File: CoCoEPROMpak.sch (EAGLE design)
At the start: 5 parts, among them P1 COCO-CART, U1 2732, U2 27128

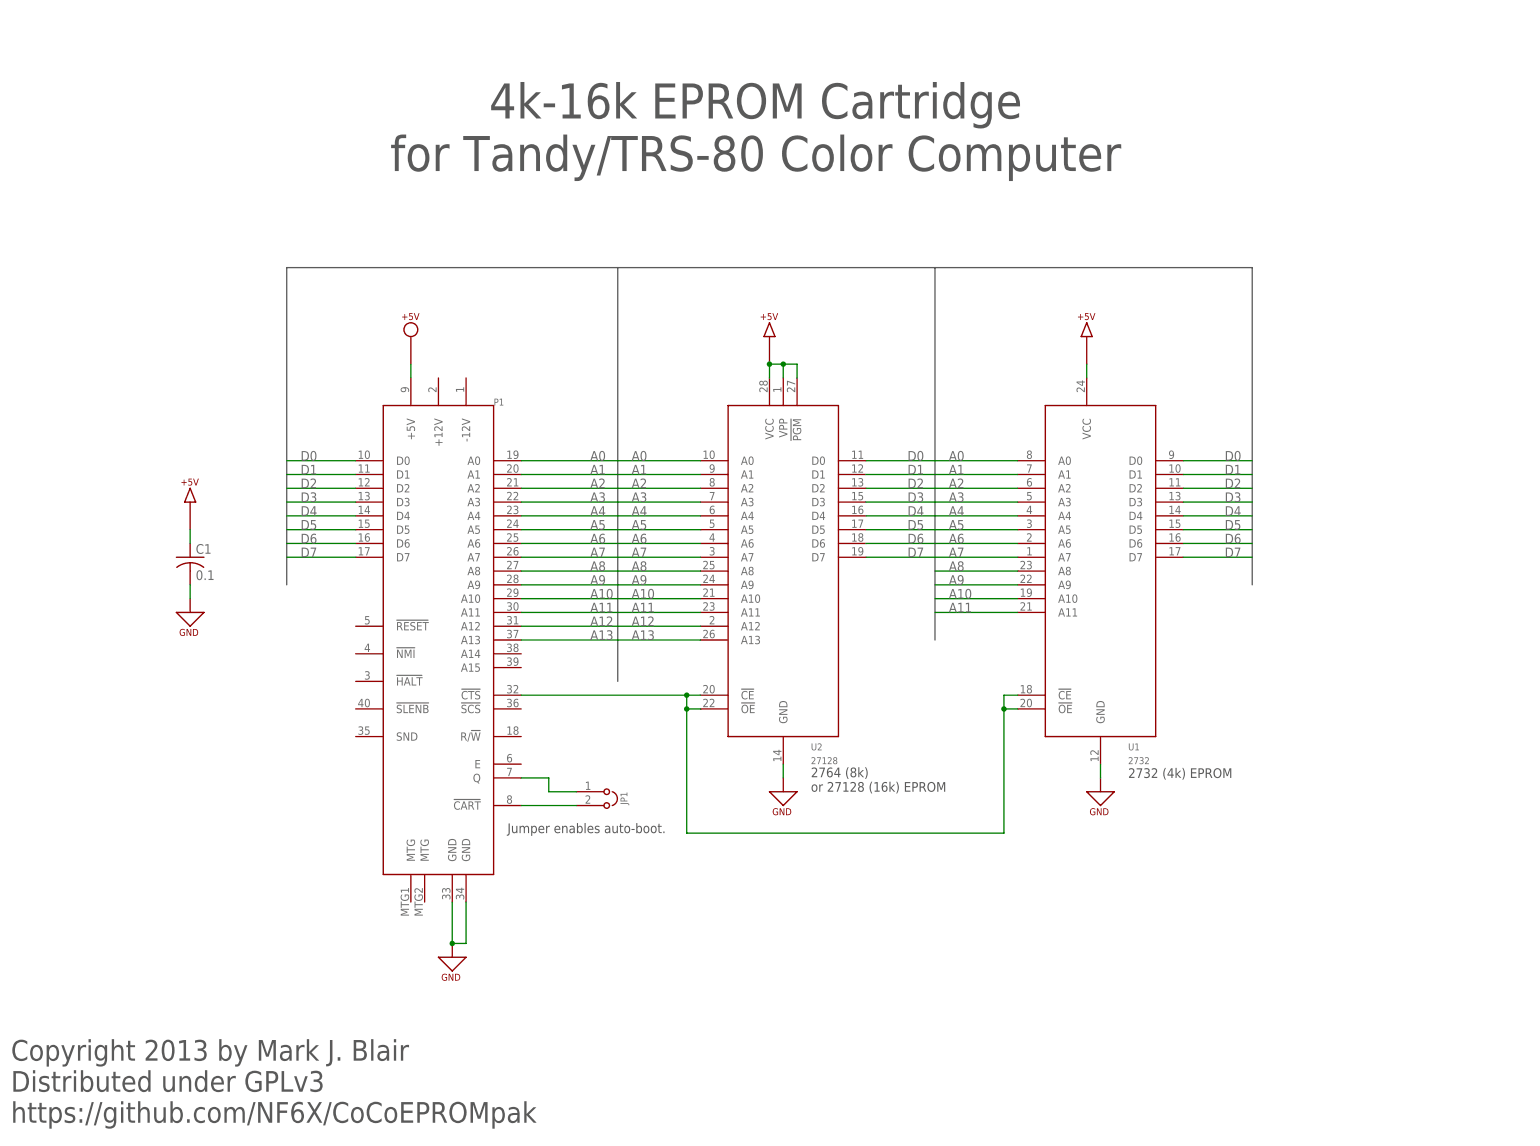
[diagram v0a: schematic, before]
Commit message: Added support for 27256 and 27512 EPROMs with bank-switching by jumper settings.
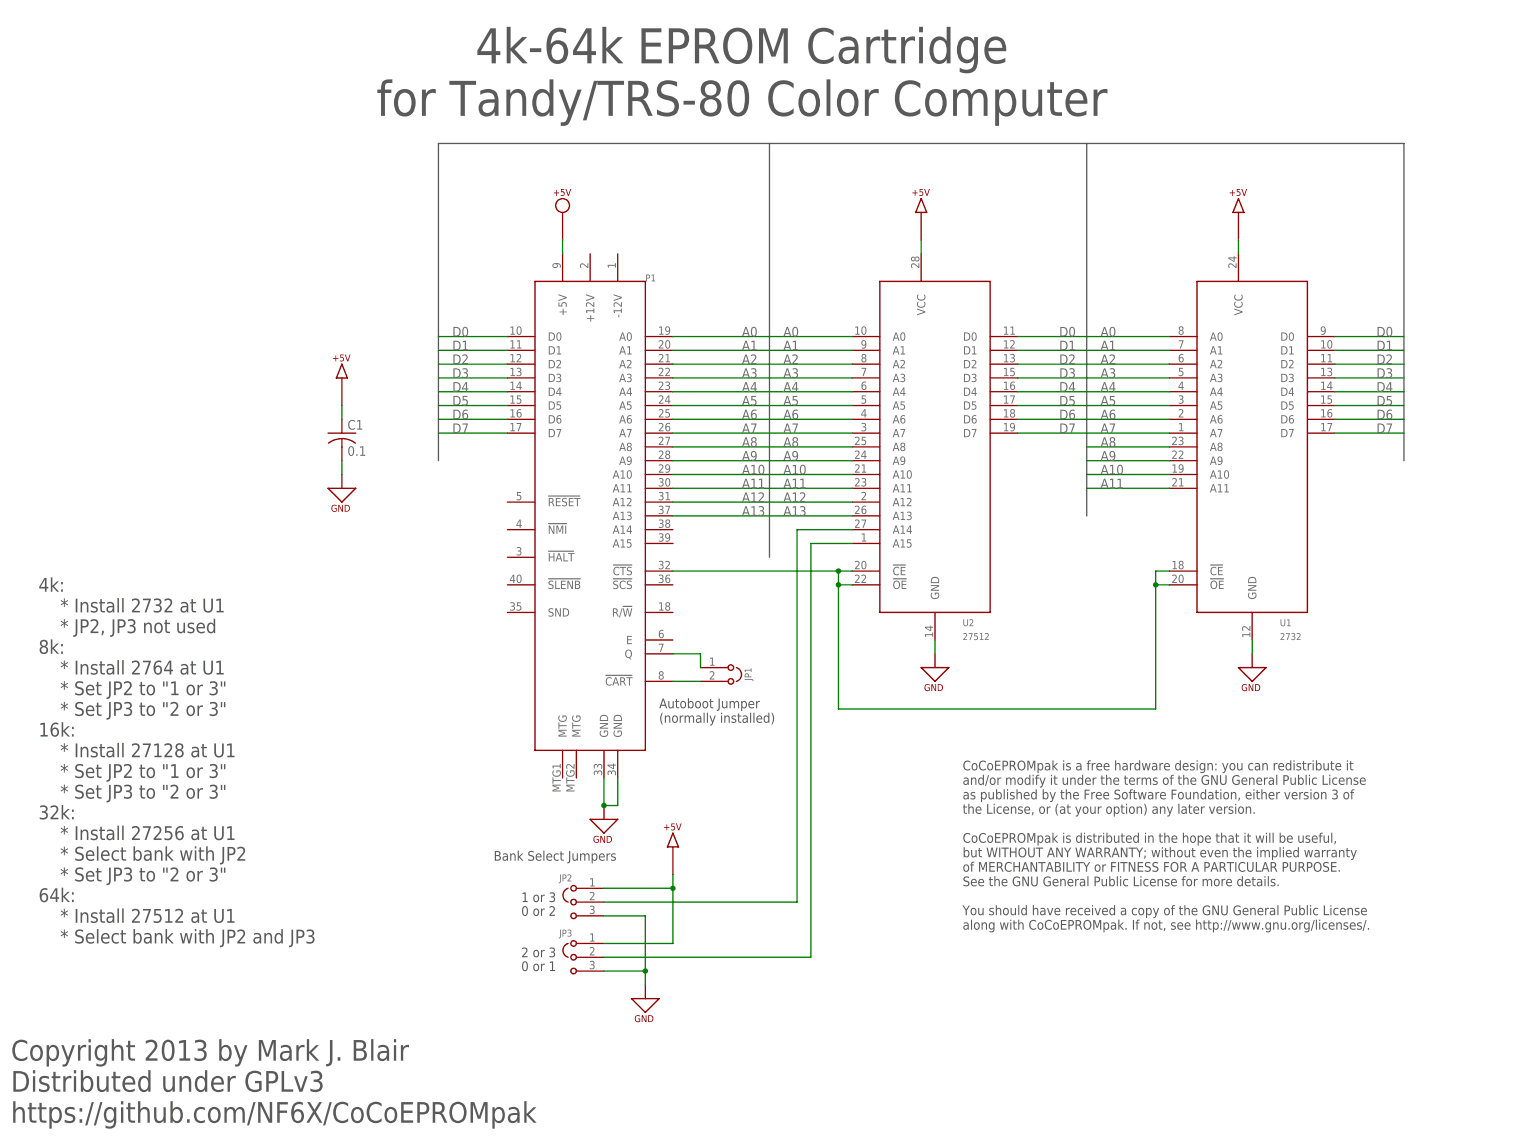
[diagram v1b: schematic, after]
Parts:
- added JP2, JP3: JP3, switch:JP3
- U2: value 27128 -> 27512; device EPROM:27128 -> EPROM:27512
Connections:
- new net N$1: JP2.2, U2.A14
- new net N$3: JP3.2, U2.A15
- net +5V: now also JP2.1, JP3.1; no longer U2.!PGM, U2.VPP
- net GND: now also JP2.3, JP3.3
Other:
- note added: "0 or 1"
- note added: "0 or 2"
- note added: "1 or 3"
- note added: "2 or 3"
- note added: "4k-64k EPROM Cartridge for Tandy/TRS-80 Color Computer"
- note added: "4k: * Install 2732 at U1 * JP2, JP3 not used 8k: * Install 2764 at U1 * Set JP2 to "1 or 3" * Set JP3 to "2 or 3" 16k: * Install 27128 at U1 * Set JP2 to "1 or 3" * Set JP3 to "2 or 3" 32k: * Install 27256 at U1 * Select bank with JP2 * Set JP3 to "2 or 3" 64k: * Install 27512 at U1 * Select bank with JP2 and JP3"
- note added: "Autoboot Jumper (normally installed)"
- note added: "Bank Select Jumpers"
- note added: "CoCoEPROMpak is a free hardware design: you can redistribute it and/or modify it under the terms of the GNU General Public License as published by the Free Software Foundation, either version 3 of the License, or (at your option) any later version. CoCoEPROMpak is distributed in the hope that it will be useful, but WITHOUT ANY WARRANTY; without even the implied warranty of MERCHANTABILITY or FITN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"
- note removed: "2732 (4k) EPROM"
- note removed: "2764 (8k) or 27128 (16k) EPROM"
- note removed: "4k-16k EPROM Cartridge for Tandy/TRS-80 Color Computer"
- note removed: "Jumper enables auto-boot."
- moved on the sheet: C1, JP1, P1, U1, U2

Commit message: Corrected reference designators in configuration documentation on schematic.
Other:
- note added: "4k: * Install 2732 at U1 * JP2, JP3 not used 8k: * Install 2764 at U2 * Set JP2 to "1 or 3" * Set JP3 to "2 or 3" 16k: * Install 27128 at U2 * Set JP2 to "1 or 3" * Set JP3 to "2 or 3" 32k: * Install 27256 at U2 * Select bank with JP2 * Set JP3 to "2 or 3" 64k: * Install 27512 at U2 * Select bank with JP2 and JP3"
- note removed: "4k: * Install 2732 at U1 * JP2, JP3 not used 8k: * Install 2764 at U1 * Set JP2 to "1 or 3" * Set JP3 to "2 or 3" 16k: * Install 27128 at U1 * Set JP2 to "1 or 3" * Set JP3 to "2 or 3" 32k: * Install 27256 at U1 * Select bank with JP2 * Set JP3 to "2 or 3" 64k: * Install 27512 at U1 * Select bank with JP2 and JP3"
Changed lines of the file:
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@@
     * JP2, JP3 not used
 8k:
-    * Install 2764 at U1
+    * Install 2764 at U2
     * Set JP2 to "1 or 3"
     * Set JP3 to "2 or 3"
 16k:
-    * Install 27128 at U1
+    * Install 27128 at U2
     * Set JP2 to "1 or 3"
     * Set JP3 to "2 or 3"
 32k:
-    * Install 27256 at U1
+    * Install 27256 at U2
     * Select bank with JP2
     * Set JP3 to "2 or 3"
 64k:
-    * Install 27512 at U1
+    * Install 27512 at U2
     * Select bank with JP2 and JP3
 </text>

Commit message: Documentation improvements.
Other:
- note added: "4k: * Install 2732 at U1 * JP2, JP3 not used 8k: * Install 2764 at U2 * Set JP2 to 1 * Set JP3 to 1 16k: * Install 27128 at U2 * Set JP2 to 1 * Set JP3 to 1 32k: * Install 27256 at U2 * Select 16k bank with JP2 * Set JP3 to 1 64k: * Install 27512 at U2 * Select 16k banks with JP2 and JP3"
- note added: "A14/!PGM!: 1 0"
- note added: "A15/VPP: 1 0"
- note added: "Autostart Jumper (normally installed)"
- note removed: "0 or 1"
- note removed: "0 or 2"
- note removed: "1 or 3"
- note removed: "2 or 3"
- note removed: "4k: * Install 2732 at U1 * JP2, JP3 not used 8k: * Install 2764 at U2 * Set JP2 to "1 or 3" * Set JP3 to "2 or 3" 16k: * Install 27128 at U2 * Set JP2 to "1 or 3" * Set JP3 to "2 or 3" 32k: * Install 27256 at U2 * Select bank with JP2 * Set JP3 to "2 or 3" 64k: * Install 27512 at U2 * Select bank with JP2 and JP3"
- note removed: "Autoboot Jumper (normally installed)"
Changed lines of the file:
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@@
 &lt;P&gt;You should have received a copy of the GNU General Public License along with CoCoEPROMpak. If not, see &lt;http://www.gnu.org/licenses/&gt;.</description>
 <plain>
-<text x="127" y="78.74" size="1.778" layer="97">Autoboot Jumper
+<text x="127" y="78.74" size="1.778" layer="97">Autostart Jumper
 (normally installed)</text>
 <text x="142.24" y="190.5" size="6.4516" layer="97" align="bottom-center">4k-64k EPROM Cartridge
@@
 https://github.com/NF6X/CoCoEPROMpak</text>
 <text x="96.52" y="53.34" size="1.778" layer="97">Bank Select Jumpers</text>
-<text x="101.6" y="43.18" size="1.778" layer="97">0 or 2</text>
-<text x="101.6" y="45.72" size="1.778" layer="97">1 or 3</text>
-<text x="101.6" y="33.02" size="1.778" layer="97">0 or 1</text>
-<text x="101.6" y="35.56" size="1.778" layer="97">2 or 3</text>
-<text x="12.7" y="38.1" size="2.54" layer="97" font="fixed">4k:
+<text x="10.16" y="60.96" size="2.54" layer="97" font="fixed">4k:
     * Install 2732 at U1
     * JP2, JP3 not used
 8k:
     * Install 2764 at U2
-    * Set JP2 to "1 or 3"
-    * Set JP3 to "2 or 3"
+    * Set JP2 to 1
+    * Set JP3 to 1
 16k:
     * Install 27128 at U2
-    * Set JP2 to "1 or 3"
-    * Set JP3 to "2 or 3"
+    * Set JP2 to 1
+    * Set JP3 to 1
 32k:
     * Install 27256 at U2
-    * Select bank with JP2
-    * Set JP3 to "2 or 3"
+    * Select 16k bank with JP2
+    * Set JP3 to 1
 64k:
     * Install 27512 at U2
-    * Select bank with JP2 and JP3
+    * Select 16k banks with JP2 and JP3
 </text>
 <text x="182.88" y="40.64" size="1.778" layer="97">CoCoEPROMpak is a free hardware design: you can redistribute it
@@
 along with CoCoEPROMpak. If not, see http://www.gnu.org/licenses/.
 </text>
+<text x="106.68" y="43.18" size="1.778" layer="97" align="bottom-right">A14/!PGM!:  1
+0</text>
+<text x="106.68" y="33.02" size="1.778" layer="97" align="bottom-right">A15/VPP:  1
+0</text>
 </plain>
 <instances>
